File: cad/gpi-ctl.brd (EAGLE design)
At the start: 75 x 73.5 mm, 101 parts, among them CN1 HEADER-1X2.4, CN2 MICROSDPLAIN, CN3 1X4-BIG, J4 1X4-BIG, SW1 SWITCHGT12-THOLE, SW2 SWITCHKMR211, SW3 SWITCHKMR211, U1 STM32F4/64, U2 ACS711, U3 ULN2003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

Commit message: labels
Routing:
- net VCCA: track 81.0 -> 82.6 mm
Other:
- board text added: "T:V12"
- board text added: "T:V3"
- board text removed: "T:Vi"
- board text removed: "T:Vr"
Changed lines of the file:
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@@
 <layer number="23" name="tOrigins" color="15" fill="1" visible="yes" active="yes"/>
 <layer number="24" name="bOrigins" color="15" fill="1" visible="yes" active="yes"/>
-<layer number="25" name="tNames" color="7" fill="1" visible="no" active="yes"/>
+<layer number="25" name="tNames" color="7" fill="1" visible="yes" active="yes"/>
 <layer number="26" name="bNames" color="7" fill="1" visible="no" active="yes"/>
 <layer number="27" name="tValues" color="7" fill="1" visible="no" active="yes"/>
@@
 <text x="67.2" y="6.9" size="1" layer="21" ratio="15">BT0</text>
 <text x="70.6" y="6.9" size="1" layer="21" ratio="15">RST</text>
-<text x="82.3" y="17.5" size="0.75" layer="21" ratio="10" rot="R45">T:Vi</text>
-<text x="82.3" y="20" size="0.75" layer="21" ratio="10" rot="R45">T:Vr</text>
-<text x="82.3" y="15" size="0.75" layer="21" ratio="10" rot="R45">T:G</text>
+<text x="81.9" y="16.8" size="0.75" layer="21" ratio="10" rot="R45">T:V12</text>
+<text x="81.9" y="19.6" size="0.75" layer="21" ratio="10" rot="R45">T:V3</text>
+<text x="81.9" y="14.7" size="0.75" layer="21" ratio="10" rot="R45">T:G</text>
 <text x="55.5" y="28.4" size="0.75" layer="21" ratio="10" rot="R45">T:Rx</text>
 <text x="56.1" y="25.8" size="0.75" layer="21" ratio="10" rot="R45">T:Tx</text>
@@
 </element>
 <element name="U2" library="jaw" package="SOIC8" value="ACS711" x="77" y="21" smashed="yes" rot="R90">
-<attribute name="NAME" x="73.005" y="23.0205" size="1" layer="25" ratio="10" rot="R180"/>
+<attribute name="NAME" x="74.805" y="24.6205" size="1" layer="25" ratio="10" rot="R180"/>
 <attribute name="VALUE" x="77" y="19.095" size="0.508" layer="27" ratio="10" rot="R90"/>
 </element>
@@
 <element name="U$1" library="jaw" package="ROBOTMAN-LOGO" value="ROBOTMAN-LOGO" x="60.5" y="44.7" rot="R270"/>
 <element name="VREG2" library="jaw" package="SOT-23-5" value="MCP1824" x="65.1" y="20.5" smashed="yes">
-<attribute name="NAME" x="63.3125" y="22.3225" size="1" layer="25" font="vector" ratio="10"/>
+<attribute name="NAME" x="63.1125" y="22.6225" size="1" layer="25" font="vector" ratio="10"/>
 <attribute name="VALUE" x="63.195" y="17.071" size="1.27" layer="27" font="vector" ratio="10" display="off"/>
 </element>
@@
 </element>
 <element name="C37" library="jaw" package="SMD0603" value="10u" x="73.5" y="64" smashed="yes" rot="R180">
-<attribute name="NAME" x="71.778" y="64.284" size="1" layer="25" font="vector" ratio="10" rot="R180"/>
+<attribute name="NAME" x="74.978" y="66.584" size="1" layer="25" font="vector" ratio="10" rot="R180"/>
 <attribute name="VALUE" x="71.478" y="64.586" size="1" layer="27" font="vector" ratio="10" rot="R180"/>
 </element>
@@
 <attribute name="VALUE" x="50.814" y="39.078" size="1" layer="27" font="vector" ratio="10" rot="R270"/>
 </element>
-<element name="C33" library="jaw" package="SMD0603" value="1u" x="70.1" y="64"/>
+<element name="C33" library="jaw" package="SMD0603" value="1u" x="70.1" y="64" smashed="yes">
+<attribute name="NAME" x="71.478" y="66.484" size="1" layer="25" font="vector" ratio="10" rot="R180"/>
+<attribute name="VALUE" x="68.322" y="61.914" size="1" layer="27" font="vector" ratio="10"/>
+</element>
 <element name="CN1" library="jaw" package="HEADER-1X2-THM-WIDE" value="HEADER-1X2.4" x="29.5" y="47.5" rot="R270"/>
 </elements>
@@
 <wire x1="72.3" y1="14.5" x2="72.3" y2="15.3" width="0.35" layer="1"/>
 <via x="73.5" y="9.9" extent="1-16" drill="0.35"/>
-<via x="73.6" y="14.7" extent="1-16" drill="0.35"/>
+<via x="73.5" y="15.3" extent="1-16" drill="0.35"/>
 <via x="58" y="7" extent="1-16" drill="0.35"/>
 <via x="59.2" y="18.8" extent="1-16" drill="0.35"/>
@@
 <via x="82.3" y="72" extent="1-16" drill="0.35"/>
 <via x="87.3" y="66.9" extent="1-16" drill="0.35"/>
-<via x="71" y="66.2" extent="1-16" drill="0.35"/>
+<via x="71.7" y="66.4" extent="1-16" drill="0.35"/>
 <via x="66.7" y="65.1" extent="1-16" drill="0.35"/>
 <via x="54" y="57" extent="1-16" drill="0.35"/>
@@
 <wire x1="79.6" y1="30.7" x2="79.6" y2="29.2" width="0.5" layer="1"/>
 <wire x1="72.3" y1="15.3" x2="73" y2="15.3" width="0.35" layer="1"/>
-<wire x1="73" y1="15.3" x2="73.6" y2="14.7" width="0.35" layer="1"/>
+<wire x1="73" y1="15.3" x2="73.5" y2="15.3" width="0.35" layer="1"/>
 <wire x1="55.231" y1="13.663" x2="54.363" y2="13.663" width="0.3" layer="1"/>
 <wire x1="54.363" y1="13.663" x2="53.9" y2="13.2" width="0.3" layer="1"/>
@@
 <via x="60.7" y="20.1" extent="1-16" drill="0.35"/>
 <wire x1="62.1" y1="20.1" x2="60.7" y2="20.1" width="0.5" layer="1"/>
-<via x="73.5" y="30.1" extent="1-16" drill="0.35"/>
+<via x="73.3" y="29.4" extent="1-16" drill="0.35"/>
 <contactref element="J4" pad="2"/>
 <contactref element="C38" pad="2"/>
@@
 <contactref element="C33" pad="1"/>
 <contactref element="J1" pad="6"/>
-<wire x1="69.3" y1="64" x2="69.3" y2="68.16" width="0.5" layer="1"/>
-<wire x1="69.3" y1="68.16" x2="68.73" y2="68.73" width="0.5" layer="1"/>
 <wire x1="39.75" y1="35.1" x2="39.75" y2="36.45" width="0.3" layer="1"/>
 <wire x1="39.75" y1="36.45" x2="40.3" y2="37" width="0.3" layer="1"/>
@@
 <wire x1="54.4" y1="48.1" x2="64.4" y2="48.1" width="0.5" layer="16"/>
 <wire x1="64.4" y1="48.1" x2="69.4" y2="53.1" width="0.5" layer="16"/>
-<wire x1="69.4" y1="53.1" x2="69.4" y2="62.2" width="0.5" layer="16"/>
-<via x="69.4" y="62.2" extent="1-16" drill="0.35"/>
-<wire x1="69.4" y1="62.2" x2="69.4" y2="63.9" width="0.5" layer="1"/>
+<wire x1="69.4" y1="53.1" x2="69.4" y2="65.4" width="0.5" layer="16"/>
+<via x="69.4" y="65.4" extent="1-16" drill="0.35"/>
+<wire x1="69.4" y1="65.4" x2="69.4" y2="63.9" width="0.5" layer="1"/>
 <wire x1="69.4" y1="63.9" x2="69.3" y2="64" width="0.5" layer="1"/>
 <via x="40.3" y="37.7" extent="1-16" drill="0.35"/>
@@
 <wire x1="54.4" y1="48.9" x2="53.1" y2="48.9" width="0.5" layer="1"/>
 <wire x1="53.1" y1="48.9" x2="53" y2="48.8" width="0.5" layer="1"/>
+<wire x1="68.73" y1="68.73" x2="69.4" y2="68.06" width="0.5" layer="16"/>
+<wire x1="69.4" y1="68.06" x2="69.4" y2="65.4" width="0.5" layer="16"/>
 </signal>
 <signal name="N$29">

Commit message: lmp current sense
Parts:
- added C41: 1u, jaw:SMD0603
- added C42: .1u, jaw:SMD0603
- added R14: .01, jaw:SMD0603
- U2: value ACS711 -> LMP8640; device jaw:SOIC8 -> jaw:SOT-6
- moved C25 5.66 mm to (74.0, 21.0), turned to 270 degrees
- moved U$1 2.95 mm to (59.1, 47.3), turned to 0 degrees
- moved U2 1.00 mm to (77.0, 20.0), turned to 0 degrees
- moved VREG2 0.51 mm to (65.0, 21.0)
- moved C36 0.14 mm to (62.0, 21.0)
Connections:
- removed net N$32: J2.7
- removed net N$45: J2.8
- removed net N$49: J3.8
- removed net N$53: J3.7
- net ADC12I: now also U2.1; no longer U2.7
- net GND: now also C41.2, C42.2, J2.7, J2.8, J3.7, J3.8, U2.2; no longer U2.5
- net VCC: no longer C25.1, C39.1, U2.8, U5.5
- net VCCA: now also C25.1, C39.1, C41.1, C42.1, U2.6, U5.5
- net VCCM: now also R14.1; no longer U2.3
- net VIN: now also R14.2, U2.3; no longer U2.1, U2.2
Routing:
- net VCCA: track 82.6 -> 140.6 mm, vias 4 -> 7
- net VCC: track 96.3 -> 83.2 mm, vias 21 -> 18
- net GND: track 170.2 -> 161.7 mm, vias 107 -> 108
- net N$8: track 11.7 -> 7.69 mm
- net ADC12I: track 52.4 -> 56.1 mm
- net TX: track 26.6 -> 24.6 mm
- net RX: track 26.3 -> 25.0 mm
- net VCCM: track 70.5 -> 71.0 mm
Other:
- board text added: "Pb"

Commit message: swap layers
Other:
- board text added: "GPI1 B3 Rev. 1"
- board text added: "JAW 2014-09"
- board text removed: "GPI1 B3 Rev. 0"
- board text removed: "JAW 2014-08"

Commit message: filter
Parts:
- added C43, R21: (no value), jaw:SMD0603
- moved R20 1.00 mm to (71.5, 16.2)
- moved C15 0.90 mm to (71.5, 9.00)
- moved C28 0.90 mm to (71.5, 12.6)
- moved R4 0.90 mm to (71.5, 14.4)
- moved R5 0.90 mm to (71.5, 10.8)
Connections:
- new net N$18: R21.1, U2.1
- net ADC12I: now also C43.1, R21.2; no longer U2.1
- net GND: now also C43.2
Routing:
- net N$18: track 0.00 -> 3.98 mm
- net ADC12I: track 56.1 -> 54.7 mm
- net NRST: track 117.0 -> 116.1 mm
- net GND: track 161.7 -> 162.5 mm
- net IOLED3: track 38.5 -> 37.9 mm

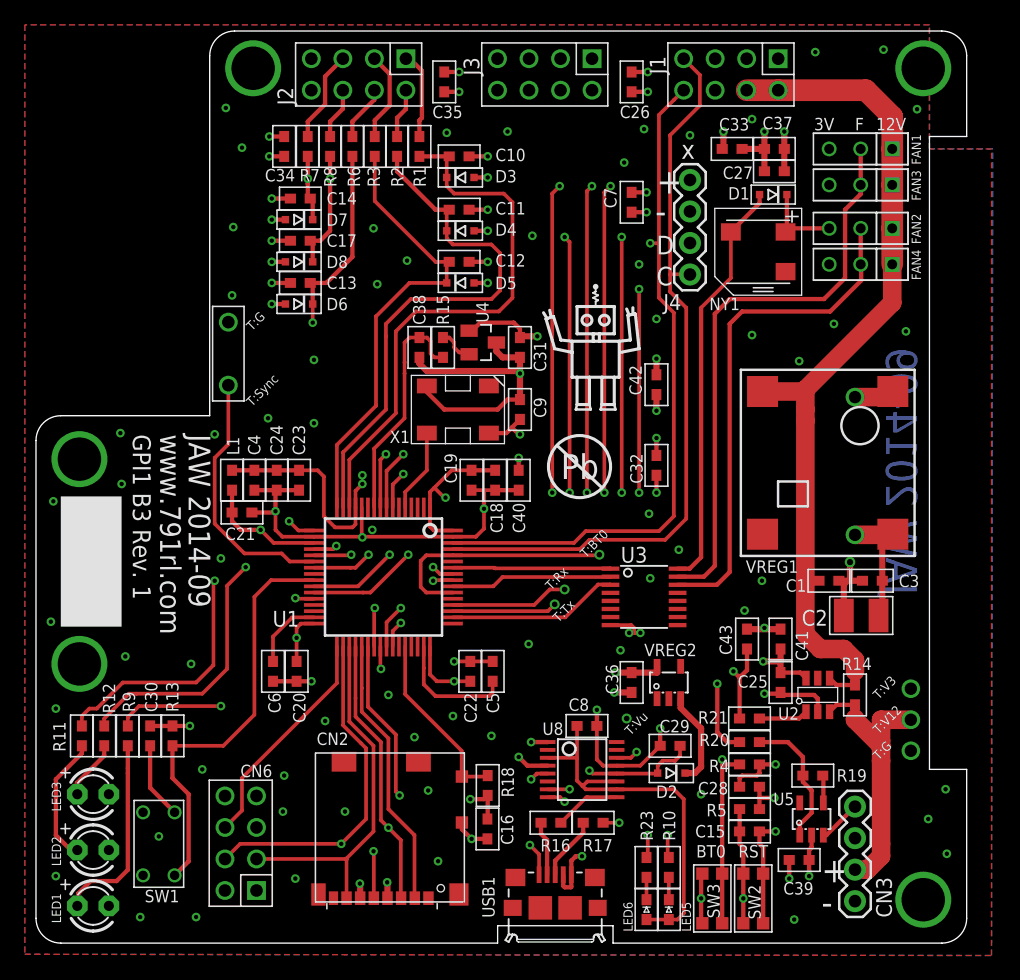
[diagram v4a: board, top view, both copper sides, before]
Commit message: output filter
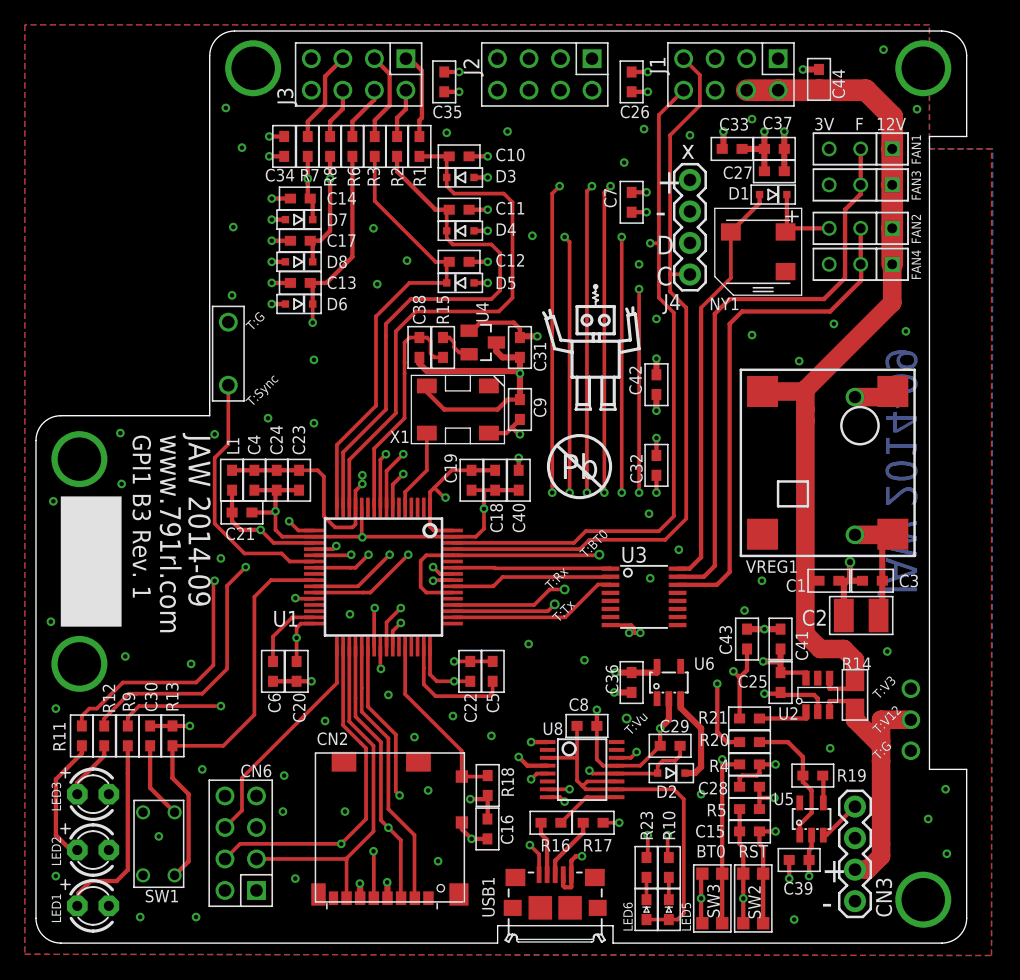
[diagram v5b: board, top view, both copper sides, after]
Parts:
- added C44: .1u 12V, jaw:SMD0603
- C1: value 10u 25V -> 10u 12V
- R14: device jaw:SMD0603 -> jaw:SMD0805
- moved J2 15.0 mm to (55.0, 70.0)
- moved J3 15.0 mm to (40.0, 70.0)
- renumbered VREG2 to U6
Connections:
- net ADC1: now also J3.1; no longer J2.1
- net ADC2: now also J3.2; no longer J2.2
- net ADC3: now also J3.3; no longer J2.3
- net ADC4: now also J3.4; no longer J2.4
- net ADC5: now also J3.5; no longer J2.5
- net ADC6: now also J3.6; no longer J2.6
- net GND: now also C44.2
- net IOG11: now also J2.3; no longer J3.3
- net IOG11N: now also J2.4; no longer J3.4
- net IOG12: now also J2.5; no longer J3.5
- net IOG12N: now also J2.6; no longer J3.6
- net IOG83: now also J2.1; no longer J3.1
- net IOG83N: now also J2.2; no longer J3.2
- net VCCM: now also C44.1
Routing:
- net GND: track 162.5 -> 166.4 mm, vias 108 -> 110
- net VCCM: track 71.0 -> 72.0 mm
- net VIN: track 22.5 -> 23.5 mm

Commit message: move leds, hole size
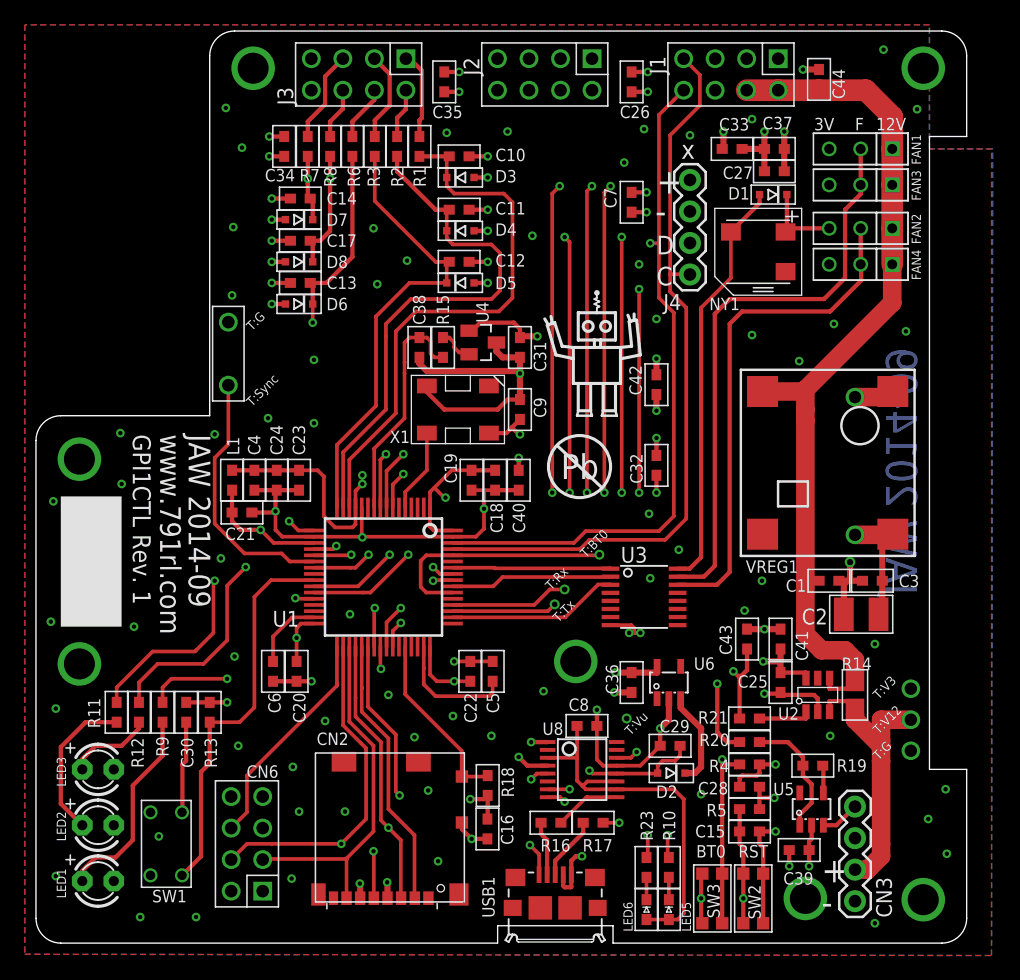
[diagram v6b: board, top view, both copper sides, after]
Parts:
- moved R13 3.55 mm to (28.0, 18.6)
- moved C30 3.47 mm to (26.1, 18.6)
- moved R11 3.38 mm to (20.5, 18.6)
- moved R12 3.38 mm to (22.3, 18.6)
- moved R9 3.38 mm to (24.2, 18.6)
- moved LED1 2.04 mm to (19.0, 5.00)
- moved LED2 2.04 mm to (19.0, 9.50)
- moved LED3 2.04 mm to (19.0, 14.0)
- moved R19 0.80 mm to (76.6, 14.3)
- moved U5 0.80 mm to (76.5, 10.8)
- moved C39 0.80 mm to (75.5, 7.50)
- moved SW1 0.60 mm to (24.5, 8.00)
- moved U$1 0.51 mm to (59.2, 46.8)
- moved CN6 0.50 mm to (31.0, 8.00)
- moved C2 0.10 mm to (80.5, 26.5)
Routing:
- net IOLED2: track 39.2 -> 34.3 mm
- net IOLED3: track 37.9 -> 33.6 mm
- net IOSWITCH1: track 33.9 -> 31.6 mm
- net N$17: track 4.82 -> 7.01 mm
- net N$16: track 10.3 -> 12.3 mm
- net IOLED1: track 24.9 -> 23.1 mm
- net VCC: track 83.2 -> 84.5 mm
- net VCCA: track 141.0 -> 139.7 mm
- net N$11: track 11.0 -> 10.2 mm
- net N$15: track 15.8 -> 16.4 mm
- net NRST: track 116.1 -> 115.5 mm
- net GND: vias 110 -> 109
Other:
- board text added: "GPI1CTL Rev. 1"
- board text removed: "GPI1 B3 Rev. 1"

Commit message: tweak
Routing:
- net GND: vias 109 -> 118
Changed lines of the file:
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@@
 <via x="22.4" y="2.1" extent="1-16" drill="0.35"/>
 <via x="23.9" y="8.6" extent="1-16" drill="0.35"/>
-<via x="15.6" y="5.4" extent="1-16" drill="0.35"/>
+<via x="15.6" y="7.4" extent="1-16" drill="0.35"/>
 <via x="46.4" y="6.6" extent="1-16" drill="0.35"/>
 <via x="50.7" y="16.7" extent="1-16" drill="0.35"/>
@@
 <wire x1="65" y1="19.7" x2="65" y2="18" width="0.5" layer="1"/>
 <wire x1="65" y1="18" x2="64.3" y2="17.3" width="0.5" layer="1"/>
-<via x="81.6" y="24.1" extent="1-16" drill="0.35"/>
+<via x="82.5" y="23.5" extent="1-16" drill="0.35"/>
 <via x="78" y="16.7" extent="1-16" drill="0.35"/>
+<via x="16.7" y="2.4" extent="1-16" drill="0.35"/>
+<via x="39.3" y="1" extent="1-16" drill="0.35"/>
+<via x="61" y="4.5" extent="1-16" drill="0.35"/>
+<via x="46.7" y="1" extent="1-16" drill="0.35"/>
+<via x="78.5" y="1.5" extent="1-16" drill="0.35"/>
+<via x="48.1" y="72.2" extent="1-16" drill="0.35"/>
+<via x="61.8" y="72.2" extent="1-16" drill="0.35"/>
+<via x="78.3" y="72.5" extent="1-16" drill="0.35"/>
+<via x="84.5" y="27.1" extent="1-16" drill="0.35"/>
 </signal>
 <signal name="VCC">
@@
 <wire x1="76.05" y1="21.8" x2="74" y2="21.8" width="0.35" layer="1"/>
 <wire x1="74" y1="17.1" x2="74" y2="21.8" width="0" layer="19" extent="1-15"/>
-<wire x1="75.55" y1="12.1" x2="74.7" y2="7.5" width="0" layer="19" extent="1-1"/>
+<wire x1="75.55" y1="12.1" x2="75" y2="16.1" width="0" layer="19" extent="1-15"/>
 </signal>
 <signal name="N$29">
@@
 <via x="57.5" y="22.7" extent="1-16" drill="2.5"/>
 </signal>
-<signal name="N$22">
-<wire x1="77.5" y1="14.3" x2="77.5" y2="12.3" width="0" layer="19" extent="1-16"/>
-</signal>
 </signals>

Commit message: tweak
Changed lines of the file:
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@@
 <layer number="3" name="Route3" color="4" fill="3" visible="no" active="no"/>
 <layer number="14" name="Route14" color="1" fill="6" visible="no" active="no"/>
-<layer number="15" name="signal" color="1" fill="1" visible="yes" active="yes"/>
-<layer number="16" name="gnd" color="6" fill="1" visible="no" active="yes"/>
+<layer number="15" name="signal" color="1" fill="1" visible="no" active="yes"/>
+<layer number="16" name="Bottom" color="6" fill="1" visible="no" active="yes"/>
 <layer number="17" name="Pads" color="2" fill="1" visible="yes" active="yes"/>
 <layer number="18" name="Vias" color="2" fill="1" visible="yes" active="yes"/>
@@
 </element>
 <element name="C39" library="jaw" package="SMD0603" value=".1u" x="75.5" y="7.5" smashed="yes">
-<attribute name="NAME" x="74.222" y="4.716" size="1" layer="25" font="vector" ratio="10"/>
+<attribute name="NAME" x="74.122" y="5.416" size="1" layer="25" font="vector" ratio="10"/>
 <attribute name="VALUE" x="73.722" y="5.414" size="1" layer="27" font="vector" ratio="10"/>
 </element>
@@
 <wire x1="65" y1="19.7" x2="65" y2="18" width="0.5" layer="1"/>
 <wire x1="65" y1="18" x2="64.3" y2="17.3" width="0.5" layer="1"/>
-<via x="82.5" y="23.5" extent="1-16" drill="0.35"/>
+<via x="81.8" y="24.1" extent="1-16" drill="0.35"/>
 <via x="78" y="16.7" extent="1-16" drill="0.35"/>
 <via x="16.7" y="2.4" extent="1-16" drill="0.35"/>
@@
 <via x="61.8" y="72.2" extent="1-16" drill="0.35"/>
 <via x="78.3" y="72.5" extent="1-16" drill="0.35"/>
-<via x="84.5" y="27.1" extent="1-16" drill="0.35"/>
+<via x="84.2" y="30.5" extent="1-16" drill="0.35"/>
 </signal>
 <signal name="VCC">
